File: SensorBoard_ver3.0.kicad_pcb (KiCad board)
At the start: 2 copper layers, 75 x 50 mm, 56 parts, among them IC1 MIC5504-3.3YM5-T5, J1 STLink, J10 Abs3, J11 Abs1, J12 Abs3, J14 Conn_01x02_Pin, J15 Conn_01x02_Pin, J2 Enc2, J3 Enc0, J4 CANConn, J5 Enc3, J6 CANConn, J7 Enc1, J8 Abs2, J9 Abs0, SW1 CAN_Terminal, SW2 IDSetSW, SW3 Reset, SW4 IDSetSW, U1 L7805, U2 MAX3485, U3 ATA6561, U4 STM32F303K8Tx, Y1 Crystal

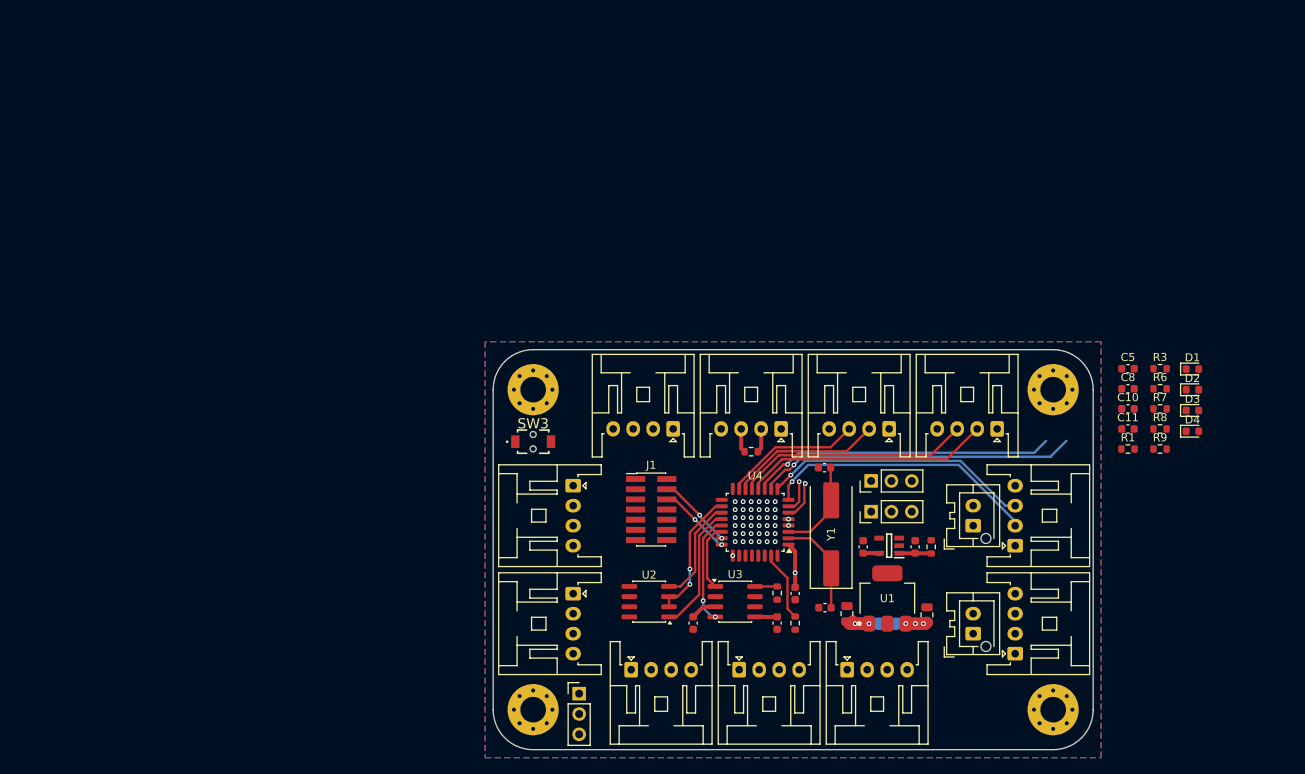
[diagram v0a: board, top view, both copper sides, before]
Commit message: コネクタを縦向きにする工事の前のコミット
コネクタを縦向きにする可能性が出てきたので、失敗したときのバックアップのためのコミット
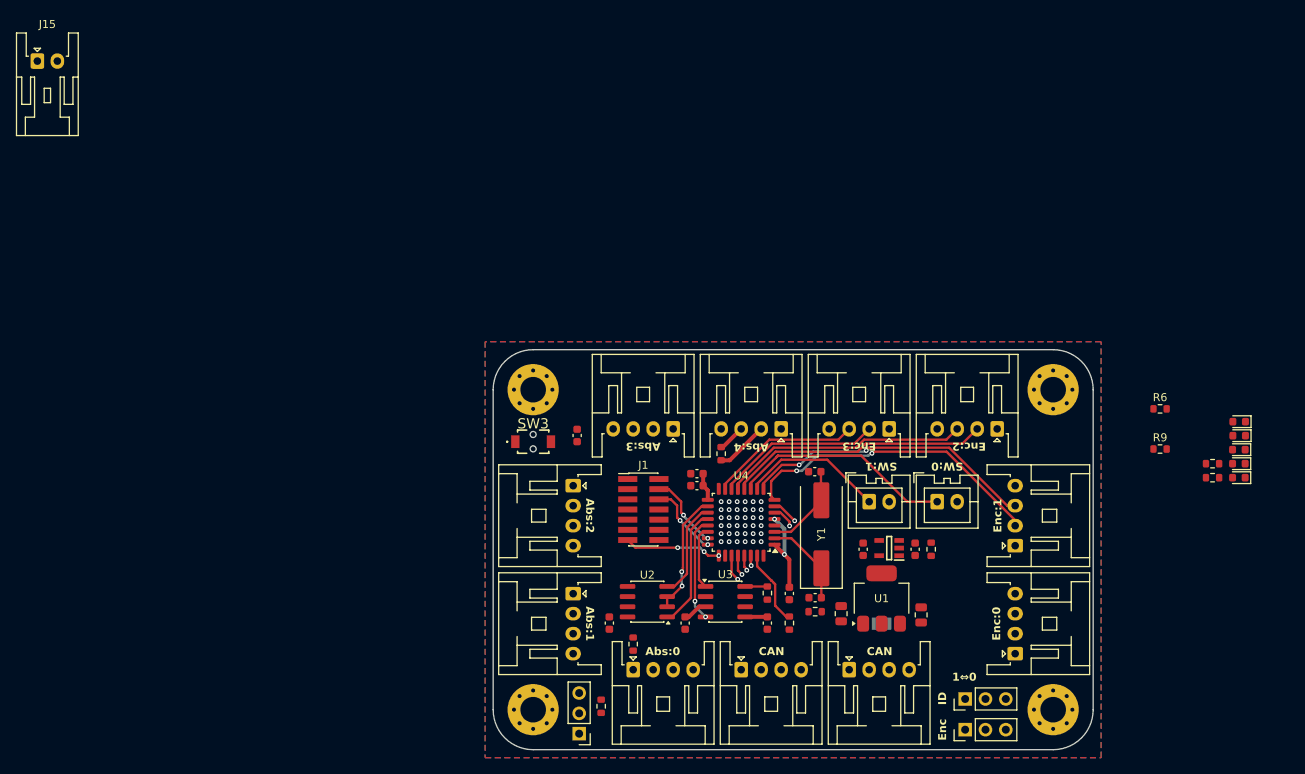
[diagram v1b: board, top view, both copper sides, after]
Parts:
- removed the J14 at (120.0, 62.0)
- added D5: LED, LED_SMD:LED_0603_1608Metric, F.Cu at (153.2, 49.0)
- added J12: Limit1, Connector_JST:JST_XA_B02B-XASK-1_1x02_P2.50mm_Vertical, F.Cu at (107.0, 59.0)
- added J13: Limit2, Connector_JST:JST_XA_B02B-XASK-1_1x02_P2.50mm_Vertical, F.Cu at (115.5, 59.0)
- added R11: 10kΩ, Resistor_SMD:R_0603_1608Metric, F.Cu at (100.2, 72.8)
- J15: value Conn_01x02_Pin -> Limit1; footprint Connector_JST:JST_XA_B02B-XASK-1-A_1x02_P2.50mm_Vertical -> Connector_JST:JST_XA_S02B-XASK-1_1x02_P2.50mm_Horizontal
- moved J15 137.1 mm to (3.02, 3.92), turned to 0 degrees
- moved R8 78.0 mm to (73.5, 84.6), turned to 90 degrees
- moved R3 74.3 mm to (77.5, 76.8), turned to -90 degrees
- moved C5 72.2 mm to (74.5, 74.2), turned to -90 degrees
- moved C10 68.9 mm to (70.5, 50.7), turned to -90 degrees
- moved C8 54.9 mm to (85.5, 55.5), turned to 180 degrees
- moved C11 54.3 mm to (85.5, 57.0), turned to 180 degrees
- moved SW2 29.7 mm to (119.0, 83.7)
- moved SW4 29.7 mm to (119.0, 87.5)
- moved D1 14.8 mm to (153.2, 56.0), turned to 180 degrees
- moved R5 11.4 mm to (149.9, 54.2)
- moved R1 11.2 mm to (149.9, 56.0)
- moved D2 10.9 mm to (153.2, 54.2), turned to 180 degrees
- moved D3 7.59 mm to (153.2, 52.5), turned to 180 degrees
- moved D4 5.86 mm to (153.2, 50.8), turned to 180 degrees
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- renumbered J11 to J10, J10 to J11, J12 to J14, J3 to J2, J2 to J3, J7 to J5, J5 to J6, J6 to J7, J9 to J8, J8 to J9, R5 to R4, R6 to R5, R7 to R6, R4 to R7
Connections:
- net /LED renamed /LED1
- J15 pad 1: unconnected-(J15-Pin_1-Pad1) -> (no net)
- J15 pad 2: unconnected-(J15-Pin_2-Pad2) -> (no net)
- U4 pad 29: unconnected-(U4-PB6-Pad29) -> /LED2
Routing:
- net /Add_PA4: track 39.8 -> 18.1 mm, vias 1 -> 0
- net /VCPRX: track 0.00 -> 12.2 mm, vias 1 -> 3
- net +5V: track 13.7 -> 3.07 mm, vias 3 -> 0
- net /Add_PA5: track 38.3 -> 28.1 mm, vias 1 -> 0
- net VCC: track 6.90 -> 0.00 mm, vias 3 -> 0
- net +3.3V: track 10.6 -> 17.3 mm
- net /EncA_1: track 34.7 -> 38.8 mm, vias 1 -> 2
- net /RS485_A: track 3.03 -> 6.63 mm
- net /EncB_1: track 33.5 -> 37.0 mm, vias 1 -> 2
- net /EncA_0: track 0.00 -> 3.27 mm, vias 0 -> 1
- net /EncB_0: track 0.00 -> 2.56 mm, vias 0 -> 1
- net /EncSW: track 5.20 -> 2.87 mm
- net /LED2: track 0.00 -> 1.95 mm, vias 0 -> 1
- net /EncA_2: track 30.9 -> 32.6 mm
- net /EncB_3: track 17.2 -> 19.0 mm
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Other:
- board text added: "${REFERENCE}"
- board text added: "1⇔0"
- board text added: "Abs:0"
- board text added: "Abs:1"
- board text added: "Abs:2"
- board text added: "Abs:3"
- board text added: "Abs:4"
- board text added: "CAN"
- board text added: "Enc"
- board text added: "Enc:0"
- board text added: "Enc:1"
- board text added: "Enc:2"
- board text added: "Enc:3"
- board text added: "ID"
- board text added: "SW:0"
- board text added: "SW:1"

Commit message: 佐渡のパソコンで操作した分
うまいこといけてるかは知らん
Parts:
- removed J15: Limit1, Connector_JST:JST_XA_S02B-XASK-1_1x02_P2.50mm_Horizontal
- moved D4 39.9 mm to (119.8, 72.5), turned to 0 degrees
- moved D5 39.9 mm to (119.8, 70.7), turned to 0 degrees
- moved R9 34.3 mm to (119.8, 77.3)
- moved D3 24.3 mm to (129.0, 50.5), turned to -90 degrees
- moved D2 22.6 mm to (130.9, 50.5), turned to -90 degrees
- moved D1 20.9 mm to (133.0, 50.5), turned to -90 degrees
- moved R11 20.5 mm to (119.8, 79.0)
- moved R6 19.9 mm to (155.7, 63.0)
- moved R5 8.47 mm to (155.7, 60.5)
- moved R1 6.07 mm to (155.7, 58.0)
- moved C1 0.15 mm to (103.5, 73.2)
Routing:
- net +5V: track 3.07 -> 184.0 mm, vias 0 -> 4
- net /RS485_A: track 6.63 -> 75.7 mm
- net /RS485_B: track 3.44 -> 69.7 mm, vias 0 -> 1
- net /CANH: track 0.00 -> 54.2 mm
- net /CANL: track 0.00 -> 53.6 mm, vias 0 -> 1
- net +3.3V: track 17.3 -> 67.5 mm, vias 2 -> 7
- net /EncSW: track 2.87 -> 49.0 mm, vias 1 -> 3
- net /NRST: track 0.00 -> 46.0 mm, vias 0 -> 3
- net /IDSet: track 3.27 -> 46.0 mm, vias 1 -> 3
- net /EncB_0: track 2.56 -> 40.8 mm
- net /EncA_0: track 3.27 -> 41.2 mm
- net /LED2: track 1.95 -> 35.2 mm, vias 1 -> 2
- net /LED1: track 1.27 -> 34.0 mm, vias 1 -> 2
- net VCC: track 0.00 -> 32.0 mm, vias 0 -> 3
- net /EncA_2: track 32.6 -> 47.0 mm, vias 0 -> 2
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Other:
- board text removed: "${REFERENCE}"

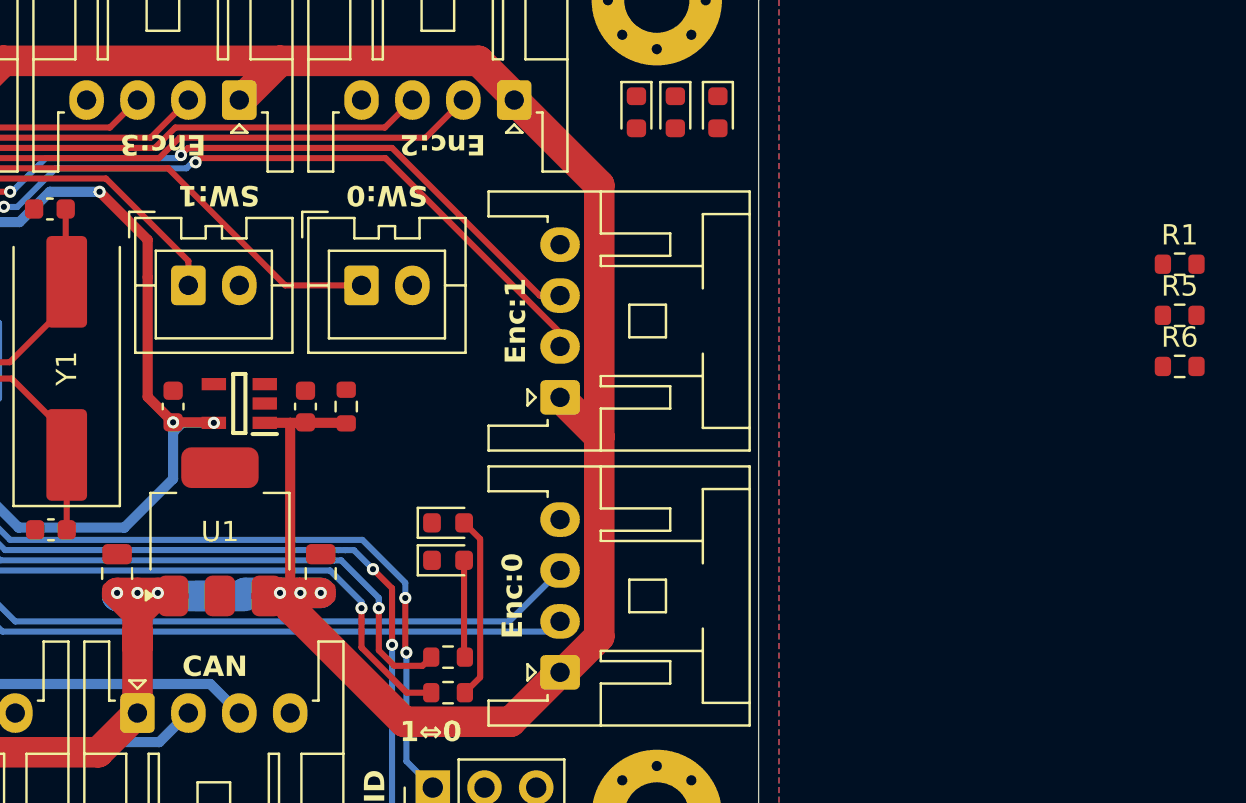
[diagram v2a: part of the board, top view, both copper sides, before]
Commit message: プロジェクトライブラリの追加・多少の進展
・プロジェクトライブラリで三端子レギュレータのフットプリントを管理した
・多少、アートワーク進めた
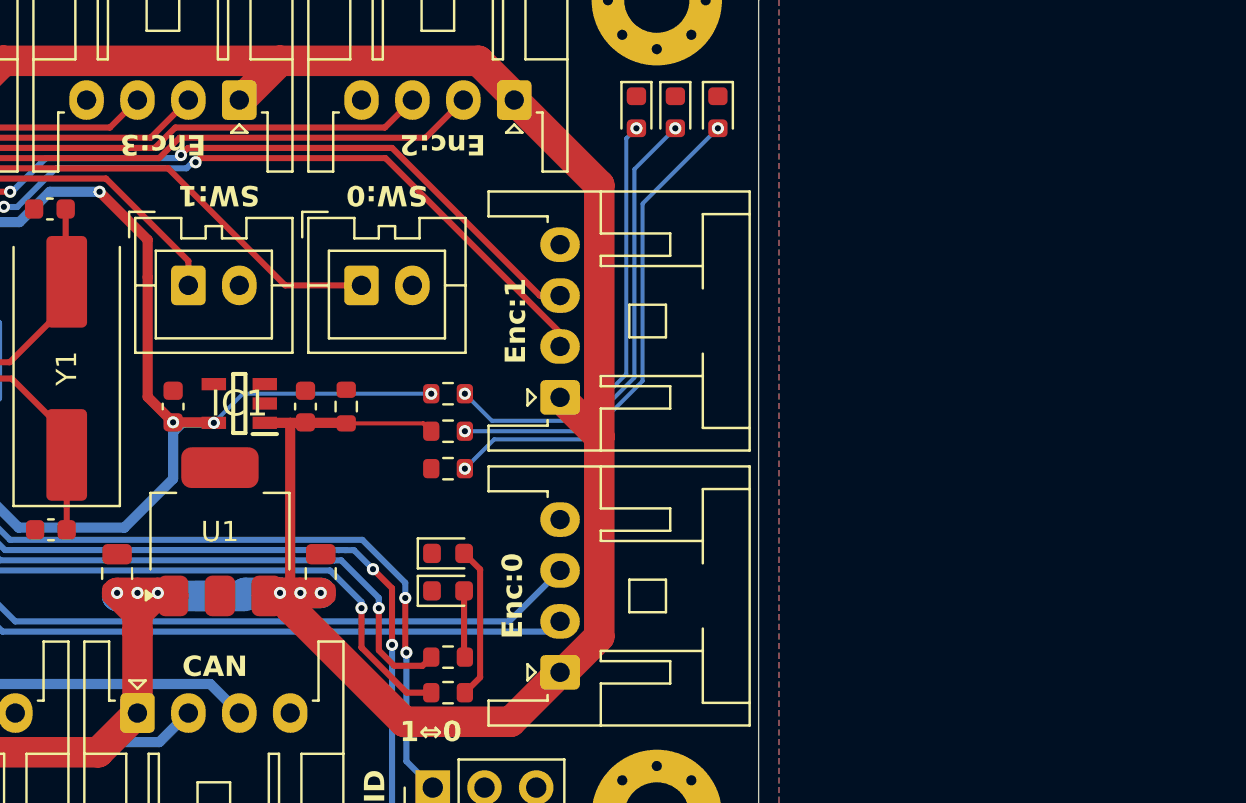
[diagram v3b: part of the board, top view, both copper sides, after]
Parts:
- IC1: footprint SOT95P280X130-5N:SOT95P280X130-5N -> SensorBoard_ver3.0:MIC5504-3.3YM5-T5
- moved R1 37.3 mm to (119.8, 68.0)
- moved R5 36.4 mm to (119.8, 66.2)
- moved R6 35.9 mm to (119.8, 64.3)
- moved D4 1.50 mm to (119.8, 74.0)
- moved D5 1.50 mm to (119.8, 72.2)
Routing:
- net Net-(D1-A): track 0.00 -> 24.4 mm, vias 0 -> 2
- net Net-(D2-A): track 0.00 -> 22.5 mm, vias 0 -> 2
- net Net-(D3-A): track 0.00 -> 21.7 mm, vias 0 -> 2
- net +3.3V: track 67.5 -> 78.7 mm, vias 7 -> 8
- net +5V: track 184.0 -> 188.4 mm
- net Net-(D4-A): track 4.77 -> 3.27 mm
- net Net-(D5-A): track 8.98 -> 7.48 mm
- net VCC: track 32.0 -> 31.2 mm
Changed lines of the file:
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@@
 	(footprint "LED_SMD:LED_0603_1608Metric"
 		(layer "F.Cu")
-		(at 119.75 70.66)
+		(at 119.75 72.16)
 		(descr "LED SMD 0603 (1608 Metric), square (rectangular) end terminal, IPC-7351 nominal, (Body size source: http://www.tortai-tech.com/upload/download/2011102023233369053.pdf), generated with kicad-footprint-generator")
 		(tags "LED")
@@
 		(tags "resistor")
 		(property "Reference" "R11"
-			(at 0 0 -0)
+			(at 0 0 0)
 			(layer "B.SilkS")
 			(effects
@@
 	(footprint "Resistor_SMD:R_0603_1608Metric"
 		(layer "F.Cu")
-		(at 155.675 62.98)
+		(at 119.75 64.32)
 		(descr "Resistor SMD 0603 (1608 Metric), square (rectangular) end terminal, IPC-7351 nominal, (Body size source: IPC-SM-782 page 72, https://www.pcb-3d.com/wordpress/wp-content/uploads/ipc-sm-782a_amendment_1_and_2.pdf), generated with kicad-footprint-generator")
 		(tags "resistor")
 		(property "Reference" "R6"
-			(at 0 -1.43 0)
-			(layer "F.SilkS")
+			(at 0 0 0)
+			(layer "B.SilkS")
 			(effects
 				(font
@@
 					(thickness 0.15)
 				)
+				(justify mirror)
 			)
 		)
@@
 			(at 0 1.43 0)
 			(layer "F.Fab")
+			(hide yes)
 			(effects
 				(font
@@
 		(tags "resistor")
 		(property "Reference" "R9"
-			(at 0 0 -0)
+			(at 0 0 0)
 			(layer "B.SilkS")
 			(effects
@@
 	(footprint "Resistor_SMD:R_0603_1608Metric"
 		(layer "F.Cu")
-		(at 155.675 60.47)
+		(at 119.75 66.16)
 		(descr "Resistor SMD 0603 (1608 Metric), square (rectangular) end terminal, IPC-7351 nominal, (Body size source: IPC-SM-782 page 72, https://www.pcb-3d.com/wordpress/wp-content/uploads/ipc-sm-782a_amendment_1_and_2.pdf), generated with kicad-footprint-generator")
 		(tags "resistor")
 		(property "Reference" "R5"
-			(at 0 -1.43 0)
-			(layer "F.SilkS")
+			(at 0 0 0)
+			(layer "B.SilkS")
 			(effects
 				(font
@@
 					(thickness 0.15)
 				)
+				(justify mirror)
 			)
 		)
@@
 			(at 0 1.43 0)
 			(layer "F.Fab")
+			(hide yes)
 			(effects
 				(font
@@
 		)
 	)
-	(footprint "SOT95P280X130-5N:SOT95P280X130-5N"
+	(footprint "SensorBoard_ver3.0:MIC5504-3.3YM5-T5"
 		(layer "F.Cu")
 		(at 109.5 64.8 180)
@@
 		(tags "Integrated Circuit")
 		(property "Reference" "IC1"
-			(at 0 0 0)
-			(layer "B.SilkS")
+			(at 0 0 180)
+			(layer "F.SilkS")
 			(effects
 				(font
@@
 					(thickness 0.254)
 				)
-				(justify mirror)
 			)
 		)
 		(property "Value" "MIC5504-3.3YM5-T5"
-			(at 0 0 0)
+			(at 0 0 180)
 			(layer "F.SilkS")
 			(hide yes)
@@
 		)
 		(property "Datasheet" "https://componentsearchengine.com/Datasheets/2/MIC5504-3.3YM5-T5.pdf"
-			(at 0 0 0)
+			(at 0 0 180)
 			(layer "F.Fab")
 			(hide yes)
@@
 		)
 		(property "Description" "LDO Voltage Regulators Single 300mA LDO"
-			(at 0 0 0)
+			(at 0 0 180)
 			(layer "F.Fab")
 			(hide yes)
@@
 			(layer "F.Fab")
 		)
+		(fp_text user "${REFERENCE}"
+			(at 0 0 180)
+			(layer "F.Fab")
+			(effects
+				(font
+					(size 1.27 1.27)
+					(thickness 0.254)
+				)
+			)
+		)
 		(pad "1" smd rect
 			(at -1.25 -0.95 270)
@@
 			(pinfunction "GND")
 			(pintype "passive")
-			(zone_connect 2)
 		)
 		(pad "3" smd rect
@@
 	(footprint "LED_SMD:LED_0603_1608Metric"
 		(layer "F.Cu")
-		(at 119.75 72.5)
+		(at 119.75 74)
 		(descr "LED SMD 0603 (1608 Metric), square (rectangular) end terminal, IPC-7351 nominal, (Body size source: http://www.tortai-tech.com/upload/download/2011102023233369053.pdf), generated with kicad-footprint-generator")
 		(tags "LED")
@@
 	(footprint "Resistor_SMD:R_0603_1608Metric"
 		(layer "F.Cu")
-		(at 155.675 57.96)
+		(at 119.75 68)
 		(descr "Resistor SMD 0603 (1608 Metric), square (rectangular) end terminal, IPC-7351 nominal, (Body size source: IPC-SM-782 page 72, https://www.pcb-3d.com/wordpress/wp-content/uploads/ipc-sm-782a_amendment_1_and_2.pdf), generated with kicad-footprint-generator")
 		(tags "resistor")
 		(property "Reference" "R1"
-			(at 0 -1.43 0)
-			(layer "F.SilkS")
+			(at 0 0 0)
+			(layer "B.SilkS")
 			(effects
 				(font
@@
 					(thickness 0.15)
 				)
+				(justify mirror)
 			)
 		)
@@
 			(at 0 1.43 0)
 			(layer "F.Fab")
+			(hide yes)
 			(effects
 				(font
@@
 	)
 	(segment
-		(start 104.5 76)
-		(end 104.5 76.75)
-		(width 1.5)
-		(layer "F.Cu")
-		(net 1)
-	)
-	(segment
 		(start 105.5 74.1)
 		(end 106.1 74.1)
@@
 	)
 	(segment
+		(start 118.925 66.16)
+		(end 118.54 65.775)
+		(width 0.2)
+		(layer "F.Cu")
+		(net 3)
+	)
+	(segment
 		(start 85.74 72.135)
 		(end 86.55 72.135)
@@
 	)
 	(segment
+		(start 118.54 65.775)
+		(end 114.75 65.775)
+		(width 0.2)
+		(layer "F.Cu")
+		(net 3)
+	)
+	(segment
 		(start 125.421999 78)
 		(end 127.176 76.245999)
@@
 	)
 	(via
+		(at 118.925 64.32)
+		(size 0.6)
+		(drill 0.3)
+		(layers "F.Cu" "B.Cu")
+		(net 4)
+	)
+	(via
 		(at 95.65 64.85)
 		(size 0.6)
@@
 	)
 	(segment
+		(start 109.68 64.32)
+		(end 108.25 65.75)
+		(width 0.2)
+		(layer "B.Cu")
+		(net 4)
+	)
+	(segment
 		(start 96.600793 63.899207)
 		(end 96.600793 62.100793)
@@
 	)
 	(segment
+		(start 118.925 64.32)
+		(end 109.68 64.32)
+		(width 0.2)
+		(layer "B.Cu")
+		(net 4)
+	)
+	(segment
 		(start 86.642729 55.892729)
 		(end 86.25 55.5)
@@
 		(net 8)
 	)
+	(via
+		(at 133 51.2875)
+		(size 0.6)
+		(drill 0.3)
+		(layers "F.Cu" "B.Cu")
+		(net 9)
+	)
+	(via
+		(at 120.575 68)
+		(size 0.6)
+		(drill 0.3)
+		(layers "F.Cu" "B.Cu")
+		(net 9)
+	)
+	(segment
+		(start 126.43436 66.561)
+		(end 129.302 63.69336)
+		(width 0.2)
+		(layer "B.Cu")
+		(net 9)
+	)
+	(segment
+		(start 122.014 66.561)
+		(end 126.43436 66.561)
+		(width 0.2)
+		(layer "B.Cu")
+		(net 9)
+	)
+	(segment
+		(start 120.575 68)
+		(end 122.014 66.561)
+		(width 0.2)
+		(layer "B.Cu")
+		(net 9)
+	)
+	(segment
+		(start 129.302 63.69336)
+		(end 129.302 54.9855)
+		(width 0.2)
+		(layer "B.Cu")
+		(net 9)
+	)
+	(segment
+		(start 129.302 54.9855)
+		(end 133 51.2875)
+		(width 0.2)
+		(layer "B.Cu")
+		(net 9)
+	)
+	(via
+		(at 120.575 66.16)
+		(size 0.6)
+		(drill 0.3)
+		(layers "F.Cu" "B.Cu")
+		(net 10)
+	)
+	(via
+		(at 130.91 51.2875)
+		(size 0.6)
+		(drill 0.3)
+		(layers "F.Cu" "B.Cu")
+		(net 10)
+	)
+	(segment
+		(start 126.26826 66.16)
+		(end 128.901 63.52726)
+		(width 0.2)
+		(layer "B.Cu")
+		(net 10)
+	)
+	(segment
+		(start 128.901 63.52726)
+		(end 128.901 53.2965)
+		(width 0.2)
+		(layer "B.Cu")
+		(net 10)
+	)
+	(segment
+		(start 120.575 66.16)
+		(end 126.26826 66.16)
+		(width 0.2)
+		(layer "B.Cu")
+		(net 10)
+	)
+	(segment
+		(start 128.901 53.2965)
+		(end 130.91 51.2875)
+		(width 0.2)
+		(layer "B.Cu")
+		(net 10)
+	)
+	(via
+		(at 129 51.2875)
+		(size 0.6)
+		(drill 0.3)
+		(layers "F.Cu" "B.Cu")
+		(net 11)
+	)
+	(via
+		(at 120.575 64.32)
+		(size 0.6)
+		(drill 0.3)
+		(layers "F.Cu" "B.Cu")
+		(net 11)
+	)
+	(segment
+		(start 128.5 63.36116)
+		(end 128.5 51.7875)
+		(width 0.2)
+		(layer "B.Cu")
+		(net 11)
+	)
+	(segment
+		(start 121.906 65.651)
+		(end 126.21016 65.651)
+		(width 0.2)
+		(layer "B.Cu")
+		(net 11)
+	)
+	(segment
+		(start 128.5 51.7875)
+		(end 129 51.2875)
+		(width 0.2)
+		(layer "B.Cu")
+		(net 11)
+	)
+	(segment
+		(start 126.21016 65.651)
+		(end 128.5 63.36116)
+		(width 0.2)
+		(layer "B.Cu")
+		(net 11)
+	)
+	(segment
+		(start 120.575 64.32)
+		(end 121.906 65.651)
+		(width 0.2)
+		(layer "B.Cu")
+		(net 11)
+	)
 	(segment
 		(start 90.365 72.135)
@@
 	)
 	(segment
-		(start 120.5375 72.5)
-		(end 120.5375 77.215987)
+		(start 120.5375 77.215987)
+		(end 120.575 77.253487)
 		(width 0.3)
 		(layer "F.Cu")
@@
 	)
 	(segment
-		(start 120.5375 77.215987)
-		(end 120.575 77.253487)
+		(start 120.5375 74)
+		(end 120.5375 77.215987)
 		(width 0.3)
 		(layer "F.Cu")
@@
 	)
 	(segment
-		(start 121.326 78.249)
-		(end 121.326 71.4485)
+		(start 121.326 72.9485)
+		(end 120.5375 72.16)
 		(width 0.3)
 		(layer "F.Cu")
@@
 	)
 	(segment
-		(start 120.575 79)
-		(end 121.326 78.249)
+		(start 121.326 78.249)
+		(end 121.326 72.9485)
 		(width 0.3)
 		(layer "F.Cu")
@@
 	)
 	(segment
-		(start 121.326 71.4485)
-		(end 120.5375 70.66)
+		(start 120.575 79)
+		(end 121.326 78.249)
 		(width 0.3)
 		(layer "F.Cu")
